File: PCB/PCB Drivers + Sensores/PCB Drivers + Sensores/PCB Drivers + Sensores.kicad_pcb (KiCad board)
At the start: 2 copper layers, 150 x 155 mm, 68 parts, among them J1 Power, J2 PWM, J3 Analog, J4 PWM, J5 Analog, J6 Communication, J7 Digital, SW1 SW_Push, U1 BOB-09056

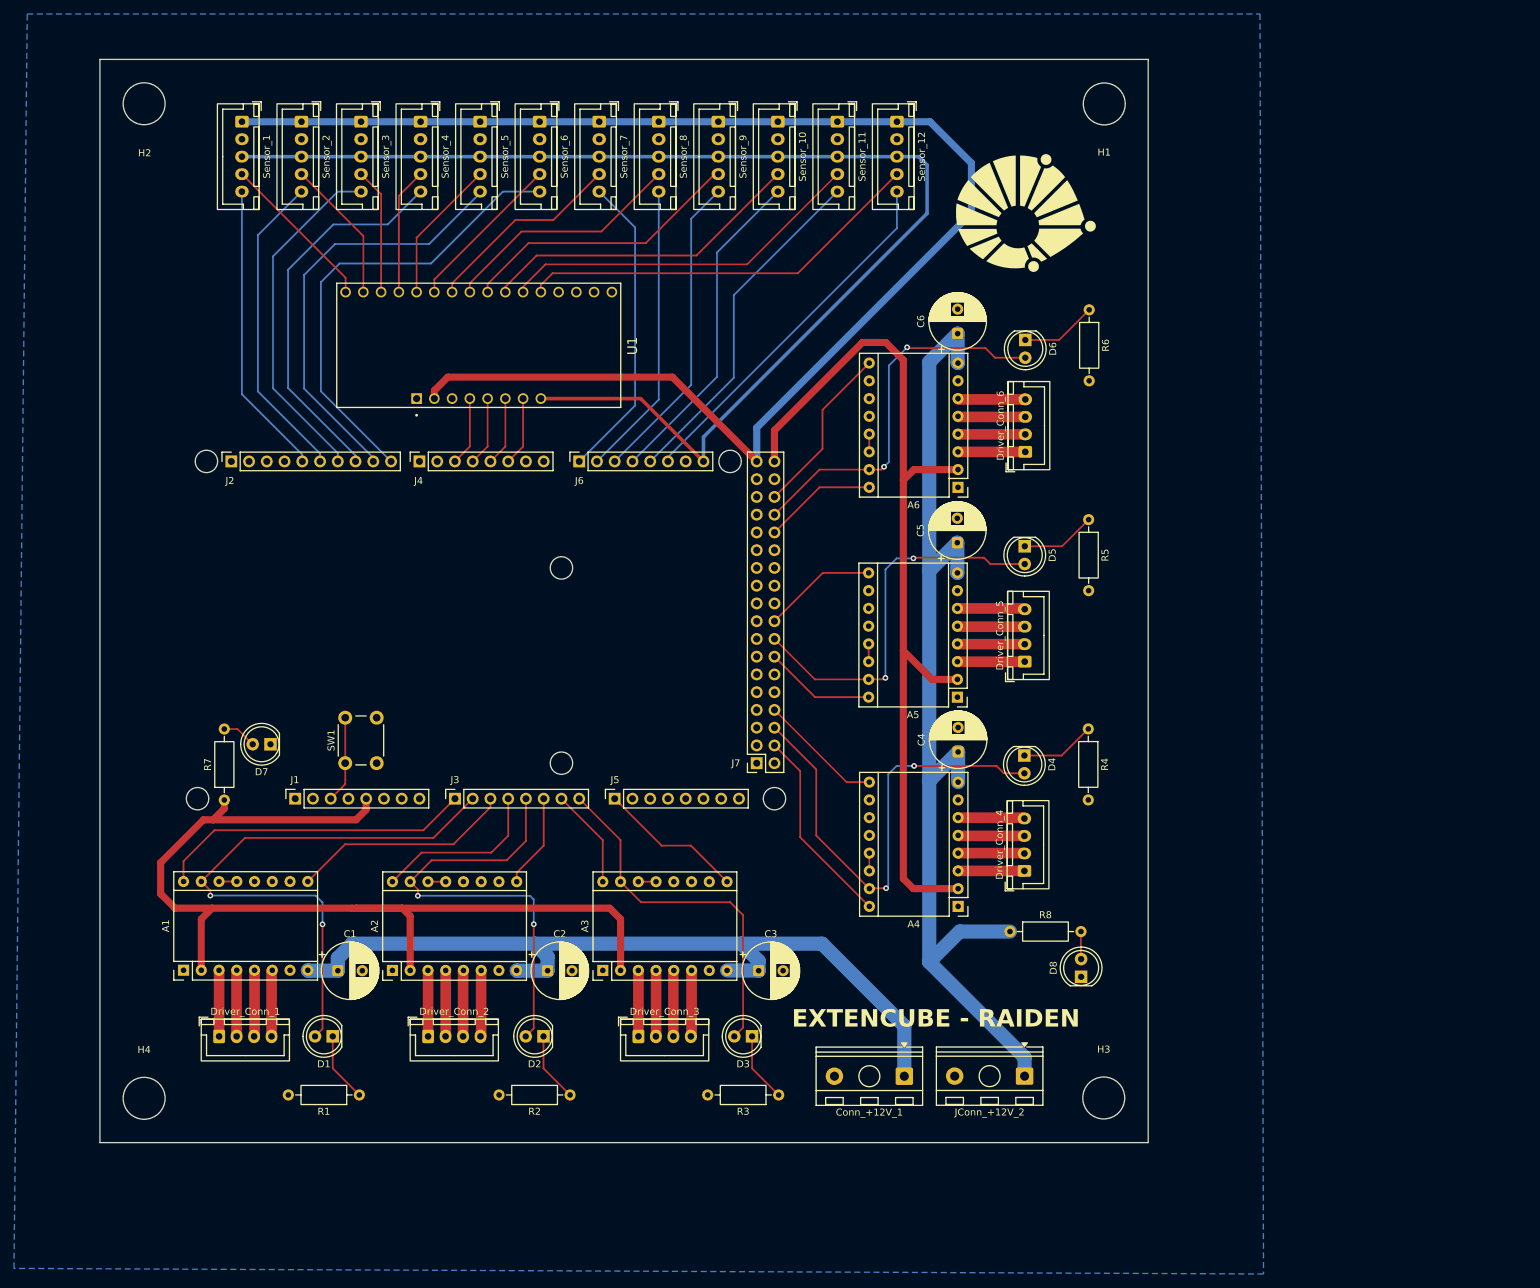
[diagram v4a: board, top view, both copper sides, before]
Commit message: +LEDs, +BARREL JACK
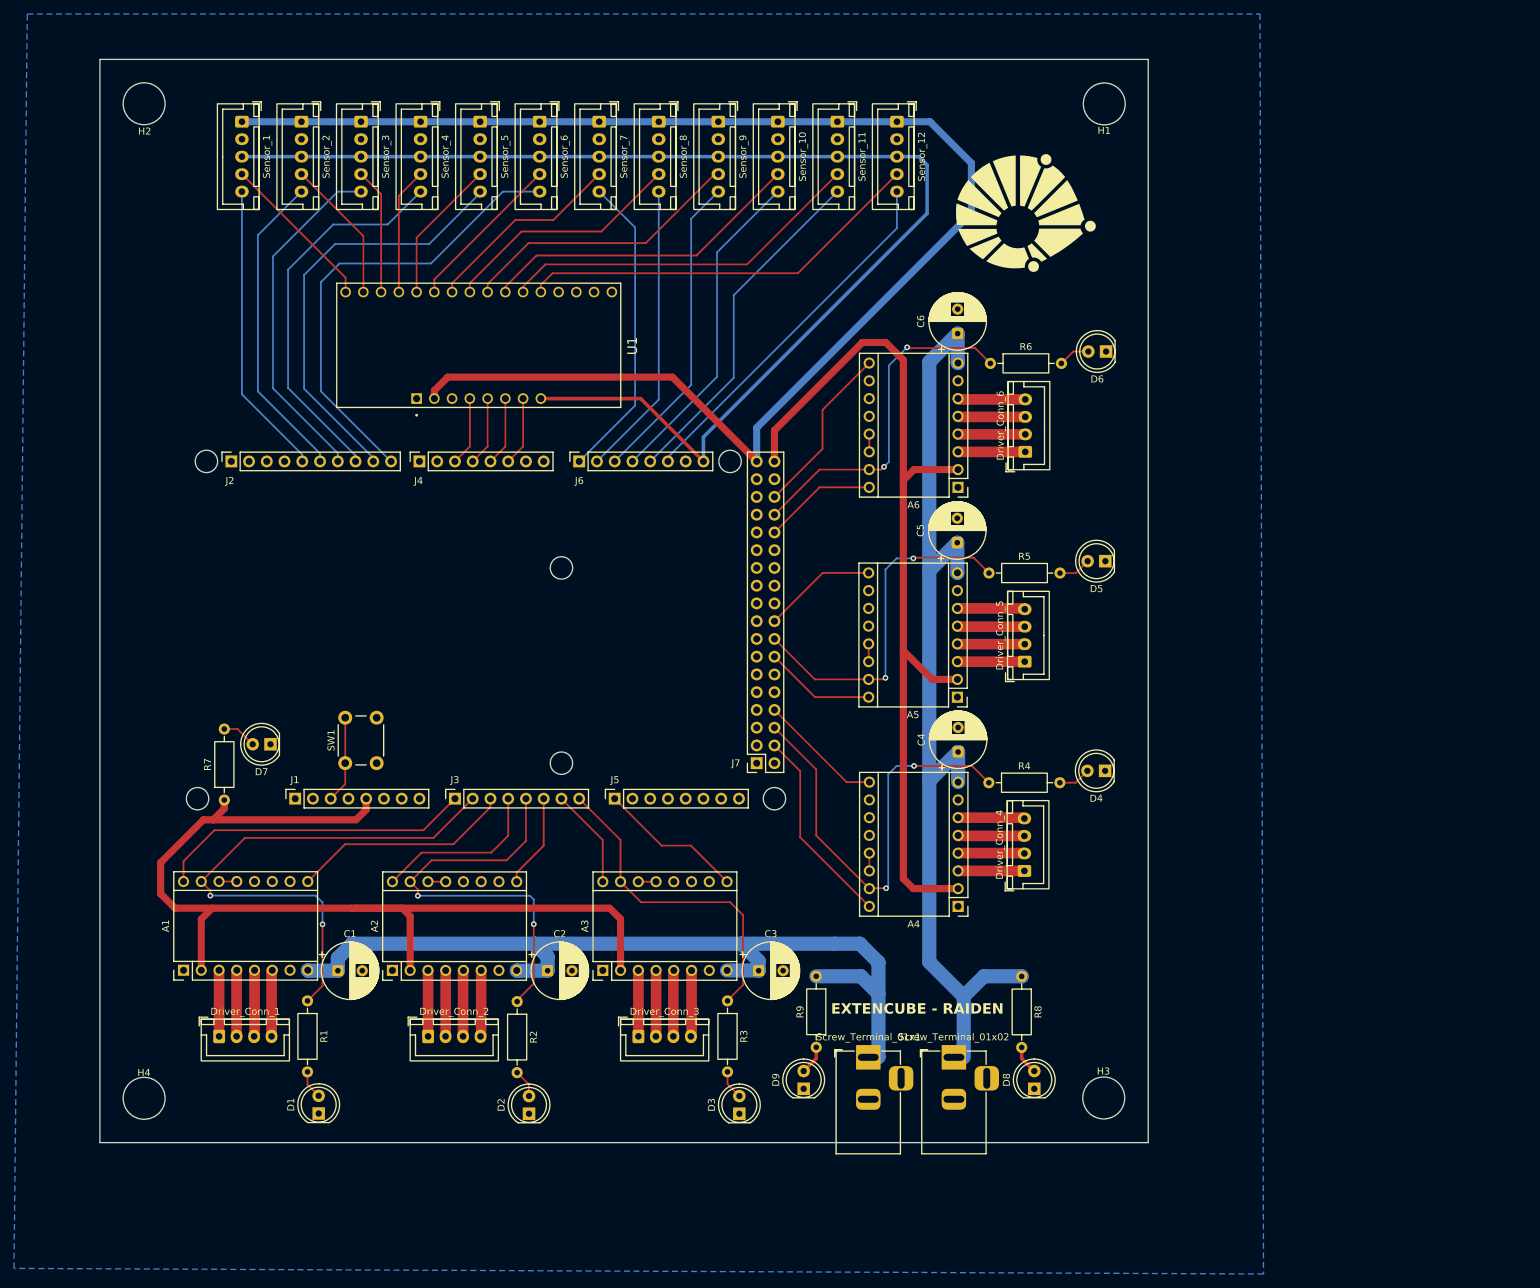
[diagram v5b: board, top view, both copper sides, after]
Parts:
- removed Conn_+12V_1, JConn_+12V_2: Screw_Terminal_01x02, TerminalBlock_RND:TerminalBlock_RND_205-00298_1x02_P10.00mm_Horizontal
- added D9: LED, LED_THT:LED_D5.0mm, F.Cu at (200.7, 207.3)
- added R9: 1k, Resistor_THT:R_Axial_DIN0207_L6.3mm_D2.5mm_P10.16mm_Horizontal, F.Cu at (202.5, 191.2)
- added Screw_Terminal_01x02: Barrel_Jack_Switch, Connector_BarrelJack:BarrelJack_Horizontal, F.Cu at (222.2, 202.8)
- added Screw_Terminal_01x1: Barrel_Jack_Switch, Connector_BarrelJack:BarrelJack_Horizontal, F.Cu at (209.9, 202.8)
- moved D8 17.4 mm to (233.7, 207.3)
- moved R5 16.2 mm to (227.2, 133.5), turned to 0 degrees
- moved R4 16.2 mm to (227.2, 163.5), turned to 0 degrees
- moved R6 16.1 mm to (227.4, 103.5), turned to 0 degrees
- moved R1 15.4 mm to (129.7, 194.7), turned to -90 degrees
- moved R2 15.4 mm to (159.7, 194.8), turned to -90 degrees
- moved R3 15.3 mm to (189.8, 194.7), turned to -90 degrees
- moved D4 11.8 mm to (243.8, 161.8), turned to 180 degrees
- moved D5 11.7 mm to (243.9, 131.8), turned to 180 degrees
- moved D6 11.7 mm to (244.0, 101.8), turned to 180 degrees
- moved D2 11.3 mm to (161.4, 210.9), turned to 90 degrees
- moved D1 11.2 mm to (131.3, 210.8), turned to 90 degrees
- moved D3 11.2 mm to (191.5, 210.9), turned to 90 degrees
- moved R8 6.64 mm to (231.9, 191.2), turned to -90 degrees
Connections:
- D1 pad 1: Net-(D1-K) -> GND
- D1 pad 2: /A1 -> Net-(D1-A)
- D2 pad 1: Net-(D2-K) -> GND
- D2 pad 2: /A4 -> Net-(D2-A)
- D3 pad 1: Net-(D3-K) -> GND
- D3 pad 2: /A7 -> Net-(D3-A)
- D4 pad 1: Net-(D4-K) -> GND
- D4 pad 2: /51 -> Net-(D4-A)
- D5 pad 1: Net-(D5-K) -> GND
- D5 pad 2: /41 -> Net-(D5-A)
- D6 pad 1: Net-(D6-K) -> GND
- D6 pad 2: /27 -> Net-(D6-A)
- R1 pad 1: Net-(D1-K) -> /A1
- R1 pad 2: GND -> Net-(D1-A)
- R2 pad 1: Net-(D2-K) -> /A4
- R2 pad 2: GND -> Net-(D2-A)
- R3 pad 1: Net-(D3-K) -> /A7
- R3 pad 2: GND -> Net-(D3-A)
- R4 pad 1: Net-(D4-K) -> /51
- R4 pad 2: GND -> Net-(D4-A)
- R5 pad 1: Net-(D5-K) -> /41
- R5 pad 2: GND -> Net-(D5-A)
- R6 pad 1: Net-(D6-K) -> /27
- R6 pad 2: GND -> Net-(D6-A)
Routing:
- net Net-(D6-K): track 10.9 -> 0.00 mm
- net Net-(D5-K): track 10.7 -> 0.00 mm
- net Net-(D4-K): track 10.7 -> 0.00 mm
- net Net-(D3-K): track 9.96 -> 0.00 mm
- net Net-(D2-K): track 9.96 -> 0.00 mm
- net Net-(D1-K): track 9.96 -> 0.00 mm
- net /A7: track 51.7 -> 47.0 mm
- net Net-(D5-A): track 0.00 -> 4.66 mm
- net /27: track 54.5 -> 49.9 mm
- net Net-(D4-A): track 0.00 -> 4.64 mm
- net /A1: track 82.4 -> 77.7 mm
- net /41: track 54.9 -> 50.3 mm
- net Net-(D6-A): track 0.00 -> 4.56 mm
- net /51: track 67.9 -> 63.4 mm
- net /A4: track 64.4 -> 59.9 mm
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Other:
- board text removed: "colocar o outro led de +12v"
- board text removed: "inverter resistores e leds"
- board text removed: "trocar os conectores +12v"

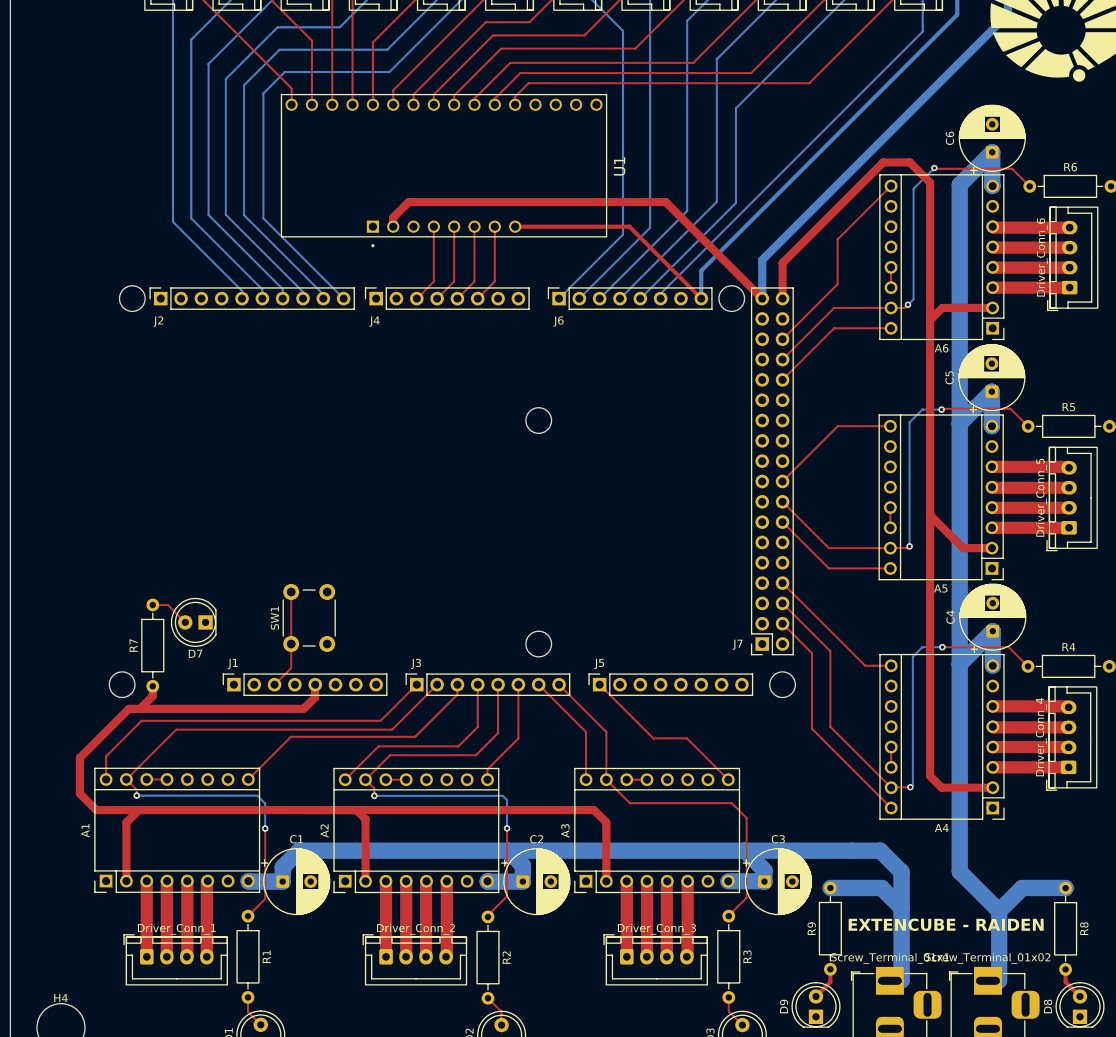
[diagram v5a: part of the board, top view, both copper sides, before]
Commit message: Logos no Silkscreen
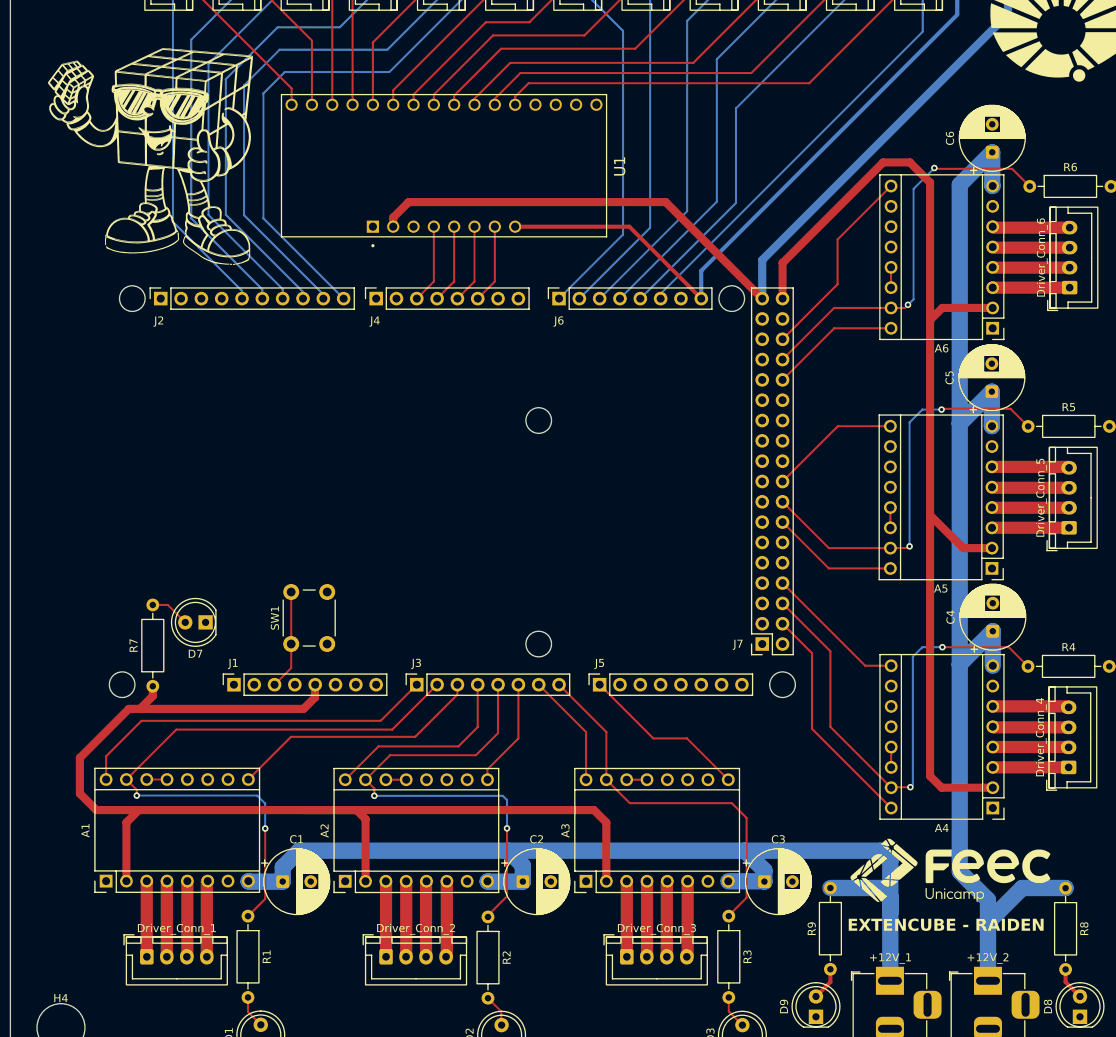
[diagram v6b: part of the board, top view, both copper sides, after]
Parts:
- added G***: LOGO, Footprints de Logos:FEEC_Logo, F.Cu at (217.5, 189.0)
- added G***: LOGO, Footprints de Logos:CubuLogo, F.Cu at (119.7, 99.2)
- renumbered Screw_Terminal_01x1 to +12V_1, Screw_Terminal_01x02 to +12V_2
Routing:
- net 12V: track 268.7 -> 269.5 mm
